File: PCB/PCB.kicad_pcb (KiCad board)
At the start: 2 copper layers, 50 parts, among them J1 USB_C_Receptacle_USB2.0_16P, J2 18650, Q1 FS8205A, SW1 SW_Push_Reset, SW2 SW_Push_Boot, U1 HT-CT62, U2 SAM-M10Q, U3 ER_OLEDM0.91_1x-I2C, U4 TPS63001, U6 BQ24074RGT, U7 DW01A, U8 USBLC6-2SC6

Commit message: started routing
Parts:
- J2: footprint Connector_JST:JST_PH_B2B-PH-K_1x02_P2.00mm_Vertical -> Battery:BatteryHolder_Keystone_1042_1x18650; moved to B.Cu
- moved Q1 166.1 mm to (189.1, 69.5)
- moved C16 148.5 mm to (198.0, 88.5), turned to 90 degrees
- moved R17 144.1 mm to (195.5, 62.0), turned to 90 degrees
- moved C18 138.2 mm to (190.2, 99.5)
- moved C20 138.0 mm to (183.5, 62.3), turned to 90 degrees
- moved C12 133.2 mm to (186.1, 99.5)
- moved R16 129.6 mm to (183.0, 66.8), turned to 90 degrees
- moved C13 123.8 mm to (162.2, 71.5)
- moved U7 117.6 mm to (189.5, 64.0)
- moved U2 116.0 mm to (187.5, 88.5), turned to 180 degrees
- moved U3 115.9 mm to (144.0, 54.7), turned to -90 degrees
- moved C9 115.2 mm to (155.2, 71.5)
- moved R14 112.4 mm to (151.7, 71.5)
- moved R19 111.4 mm to (158.7, 71.5)
- moved R9 106.8 mm to (148.2, 68.5)
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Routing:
- net GND: track 0.00 -> 69.1 mm
- net VBUS_5V: track 0.00 -> 37.2 mm
- net +BATT: track 0.00 -> 32.6 mm
- net SYS: track 0.00 -> 29.3 mm
- net Net-(J1-D--PadA7): track 0.00 -> 20.7 mm
- net Net-(J1-CC2): track 0.00 -> 7.84 mm
- net Net-(U4-EN): track 0.00 -> 6.24 mm
- net Net-(D1-K): track 0.00 -> 6.07 mm
- net Net-(J1-CC1): track 0.00 -> 5.62 mm, vias 0 -> 2
- net Net-(U4-L2): track 0.00 -> 3.85 mm
- net Net-(U4-L1): track 0.00 -> 3.85 mm
- net Net-(D1-A): track 0.00 -> 3.06 mm
- net Net-(J1-D+-PadA6): track 0.00 -> 2.71 mm
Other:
- board outline added: 100 x 50 mm

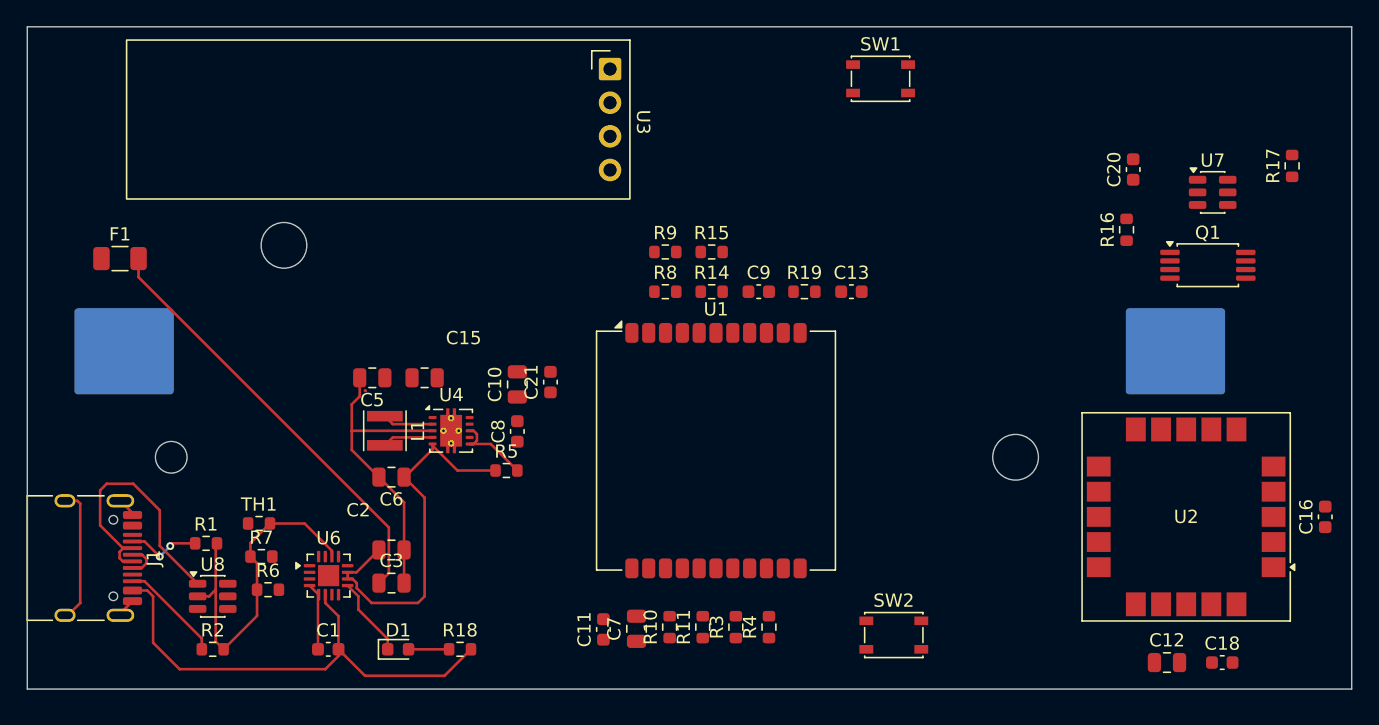
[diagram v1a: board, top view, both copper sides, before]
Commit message: finished routing, fixed drc errors
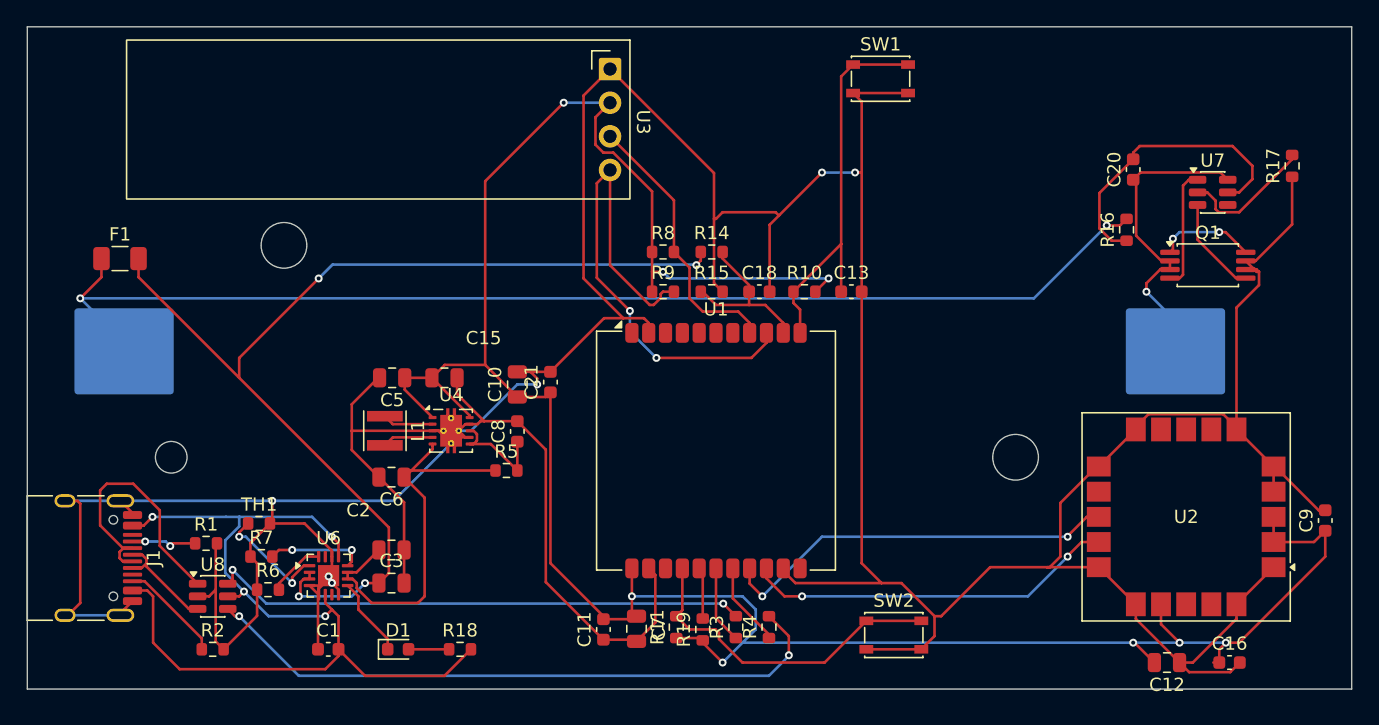
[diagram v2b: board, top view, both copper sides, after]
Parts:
- moved C9 46.1 mm to (198.0, 88.8), turned to 90 degrees
- moved C18 44.8 mm to (155.3, 71.5)
- moved R10 27.3 mm to (158.7, 71.5), turned to 0 degrees
- moved R19 26.6 mm to (151.0, 97.0), turned to 90 degrees
- moved C16 13.2 mm to (190.8, 99.5), turned to 0 degrees
- moved R8 3.01 mm to (148.0, 68.5)
- moved R9 3.01 mm to (148.0, 71.5)
- moved R14 3.00 mm to (151.7, 68.5)
- moved R15 3.00 mm to (151.7, 71.5)
- moved R11 2.00 mm to (149.0, 96.8)
- moved C15 1.50 mm to (131.5, 78.0)
- moved C5 1.50 mm to (127.5, 78.0)
- turned C12 to 180 degrees
- turned C7 to -90 degrees
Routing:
- net GND: track 69.1 -> 397.8 mm, vias 0 -> 6
- net +3V3: track 0.00 -> 185.1 mm, vias 0 -> 8
- net Net-(J2-Pin_1): track 0.00 -> 90.5 mm, vias 0 -> 2
- net +BATT: track 32.6 -> 81.6 mm, vias 0 -> 4
- net USB_D+: track 0.00 -> 48.7 mm, vias 0 -> 2
- net USB_D-: track 0.00 -> 40.7 mm, vias 0 -> 2
- net OLED_SDA: track 0.00 -> 39.8 mm, vias 0 -> 2
- net VBUS_5V: track 37.2 -> 70.5 mm, vias 0 -> 4
- net GNSS_TX: track 0.00 -> 30.5 mm, vias 0 -> 2
- net Net-(U1-EN): track 0.00 -> 30.1 mm
- net GNSS_RX: track 0.00 -> 28.2 mm, vias 0 -> 2
- net Net-(U1-GPIO9): track 0.00 -> 25.3 mm
- net Net-(J2-Pin_2): track 0.00 -> 24.1 mm, vias 0 -> 1
- net Net-(U7-VCC): track 0.00 -> 22.3 mm
- net OLED_SCL: track 0.00 -> 20.8 mm
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
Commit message: logo added
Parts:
- added G***: LOGO, KiCadLibraries:tunduk_logo, F.Cu at (172.0, 78.0)
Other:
- board text added: "1"
- board text added: "kyrg4z · mesh node v1.0"

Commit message: gerbers, firmware, and prod
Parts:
- added G***: LOGO, KiCadLibraries:ilbirs_logo, F.Cu at (126.5, 71.0)
- moved G*** 2.55 mm to (172.5, 75.5)
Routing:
- net GND: track 397.8 -> 405.0 mm
- added copper zone on F.Cu, net GND
